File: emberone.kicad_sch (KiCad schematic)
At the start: 22 parts, among them J1 Screw Terminal, J2 Screw Terminal

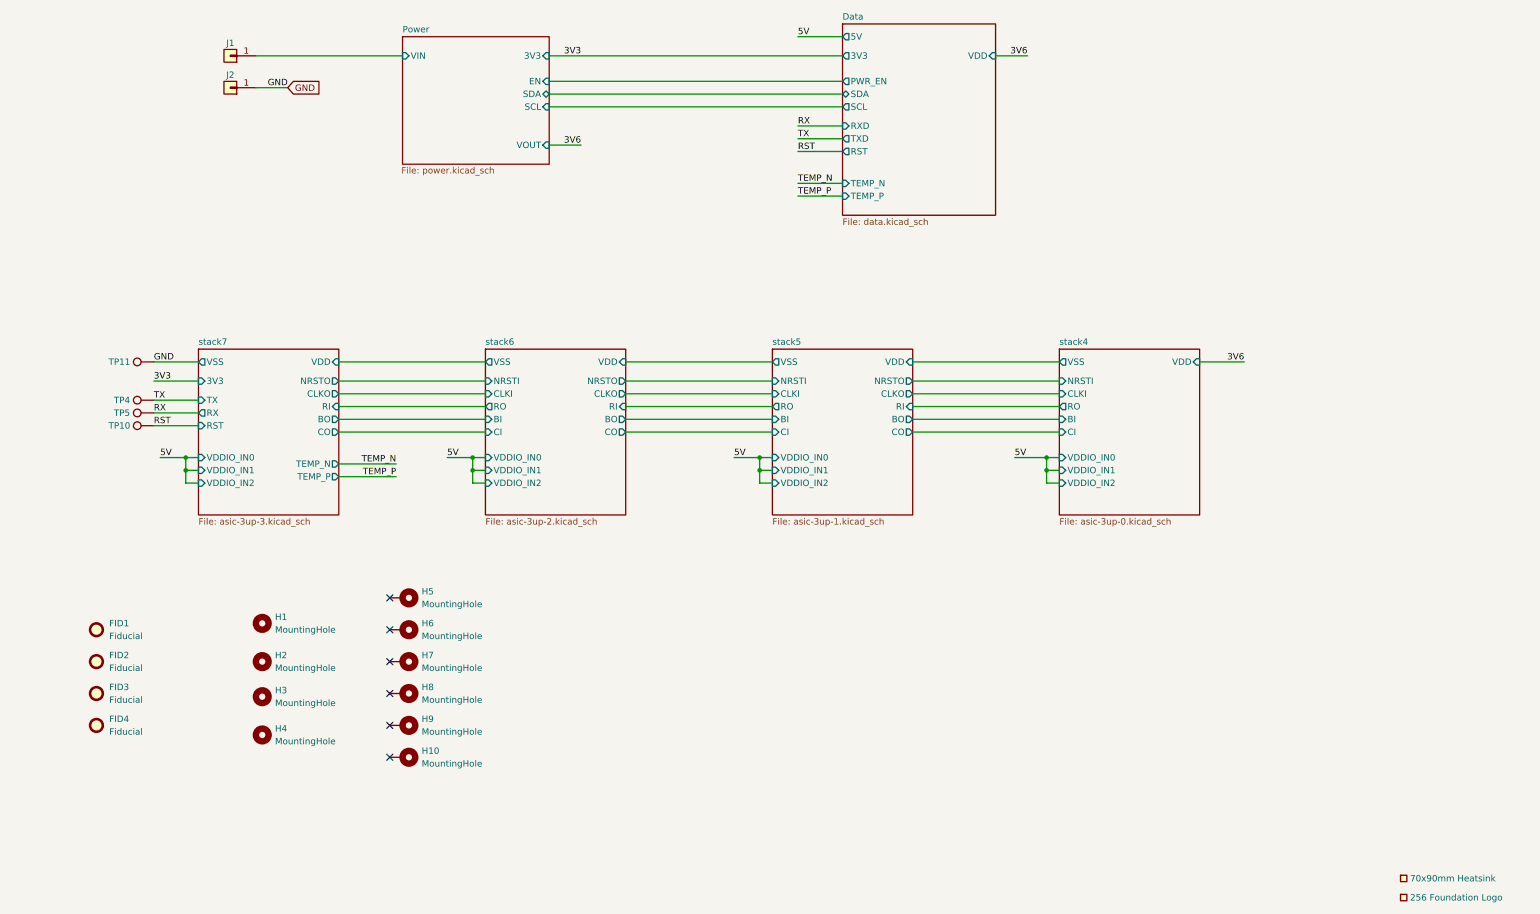
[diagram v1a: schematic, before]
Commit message: switch schematic to TPS546D24S regulator. get pcb mostly synced
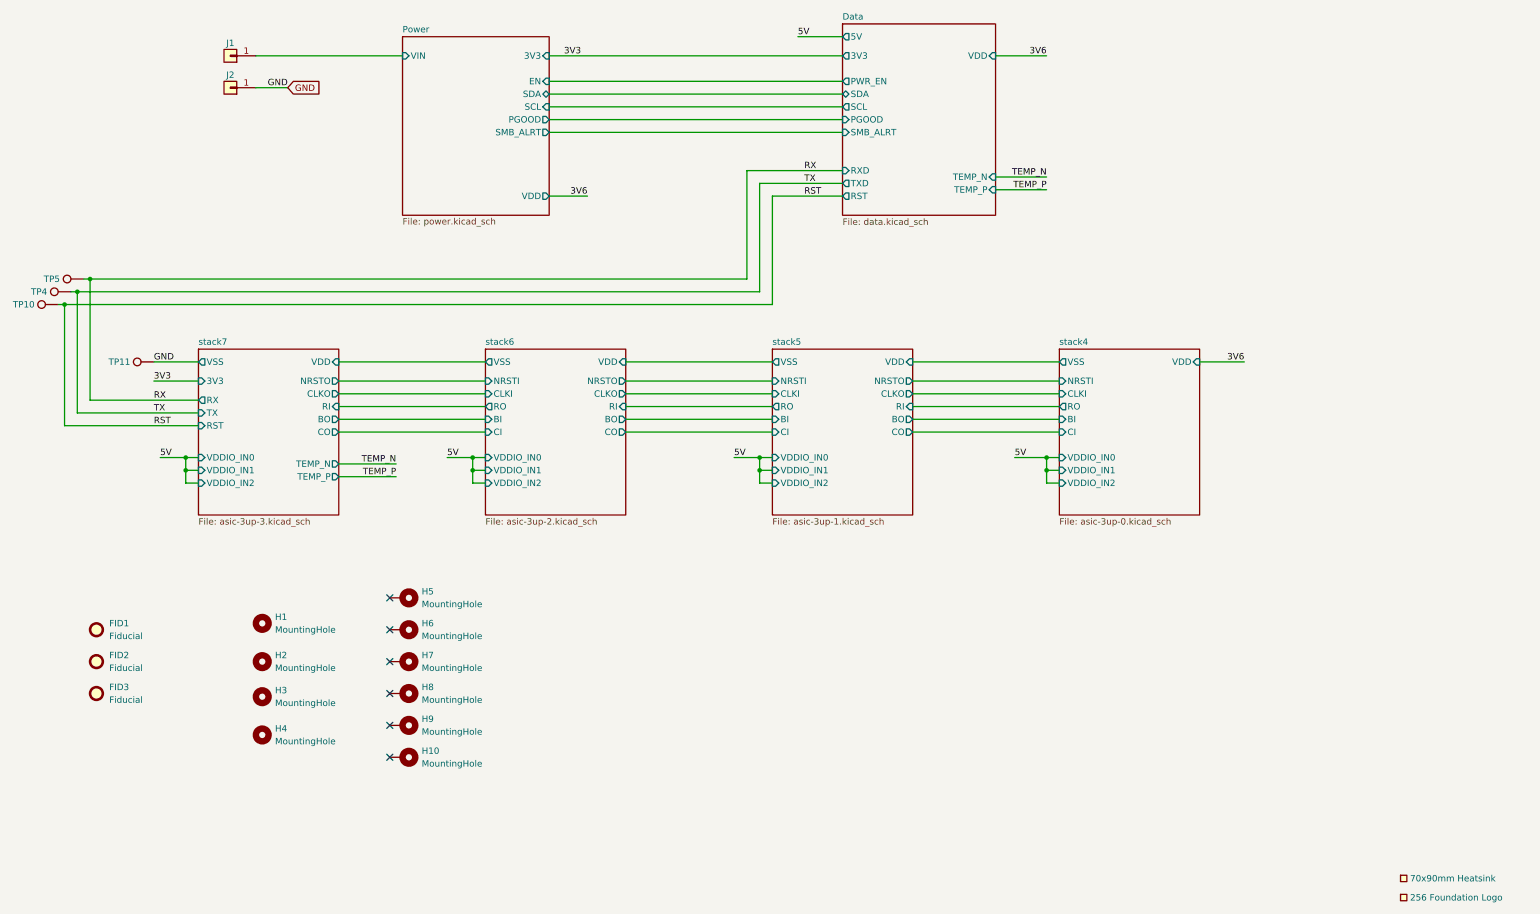
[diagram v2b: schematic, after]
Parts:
- removed FID4: Fiducial, emberone:Fiducial_1mm_Mask2mm, symbol Mechanical:Fiducial
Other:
- sheet Data ports: added PGOOD, SMB_ALRT; removed none
- sheet Power ports: added PGOOD, SMB_ALRT, VDD; removed VOUT
- moved on the sheet: TP10, TP4, TP5

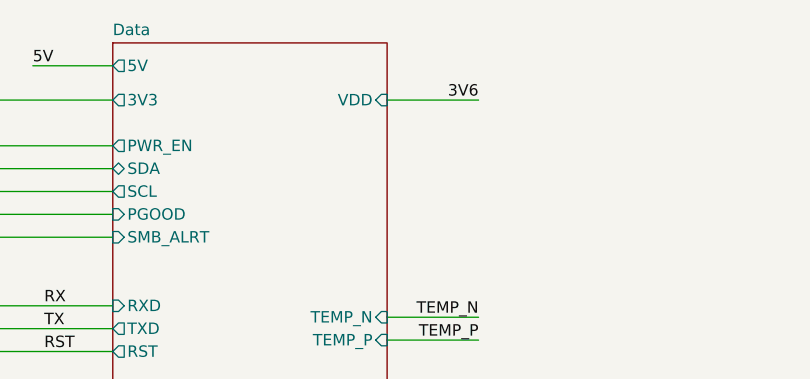
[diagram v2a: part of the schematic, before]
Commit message: mostly done routing
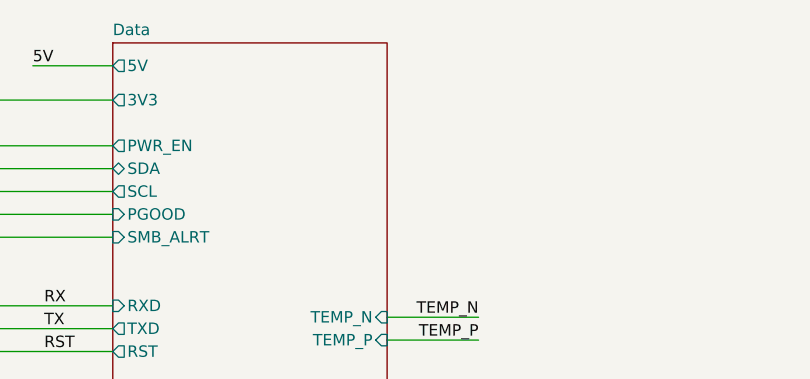
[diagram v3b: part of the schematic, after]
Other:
- sheet Data ports: added none; removed VDD
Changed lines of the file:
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@@
-	(wire
-		(pts
-			(xy 269.24 82.55) (xy 279.4 82.55)
-		)
-		(stroke
-			(width 0)
-			(type default)
-		)
-	)
 	(wire
 		(pts
@@
 			)
 			(justify left bottom)
-		)
-	)
-	(label "3V6"
-		(at 279.4 82.55 180)
-		(effects
-			(font
-				(size 1.27 1.27)
-			)
-			(justify right bottom)
 		)
 	)
@@
 			)
 		)
-		(pin "VDD" input
-			(at 269.24 82.55 0)
-			(effects
-				(font
-					(size 1.27 1.27)
-				)
-				(justify right)
-			)
-		)

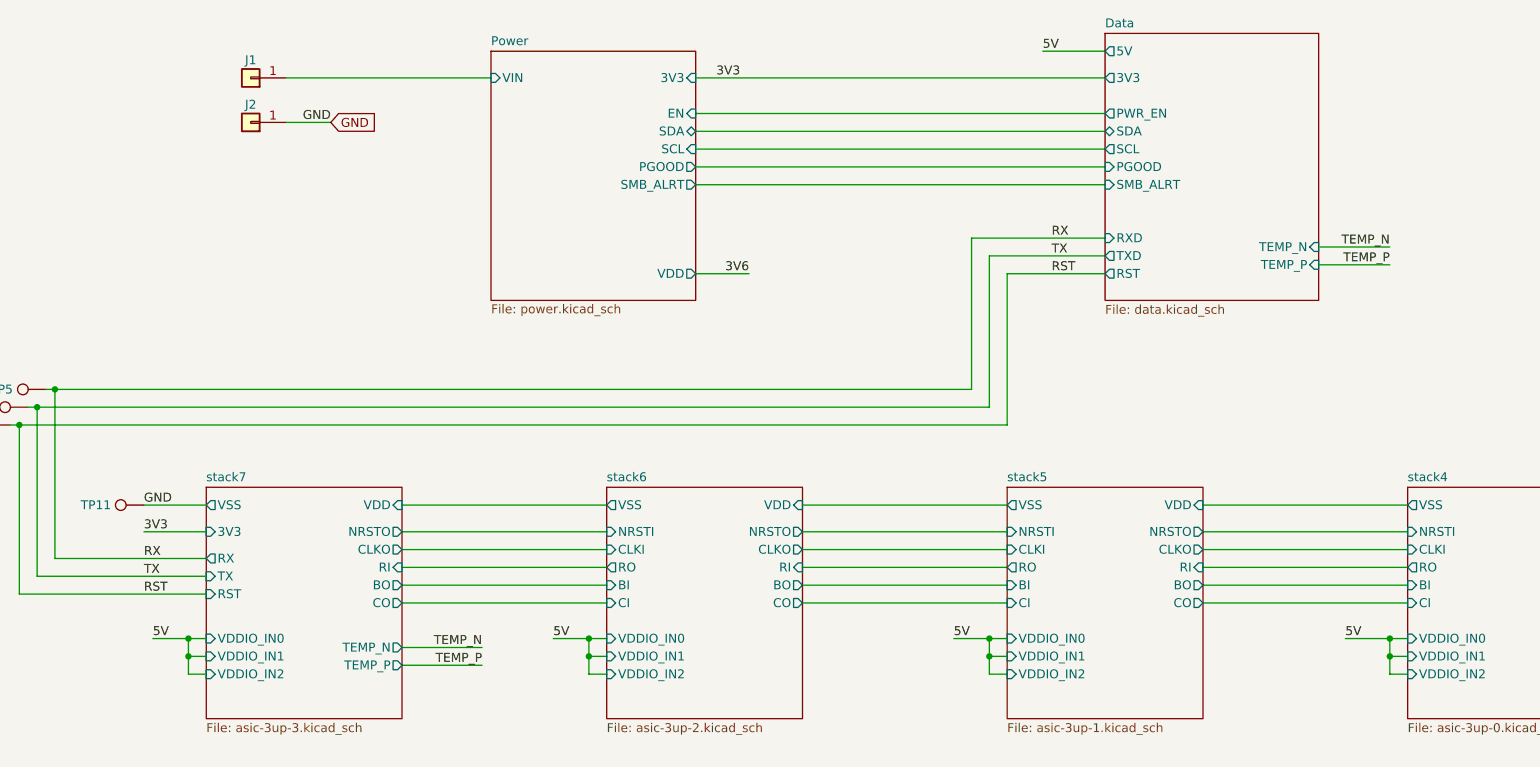
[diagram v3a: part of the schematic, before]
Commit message: Added 5V Load switch TPS22919 for #52
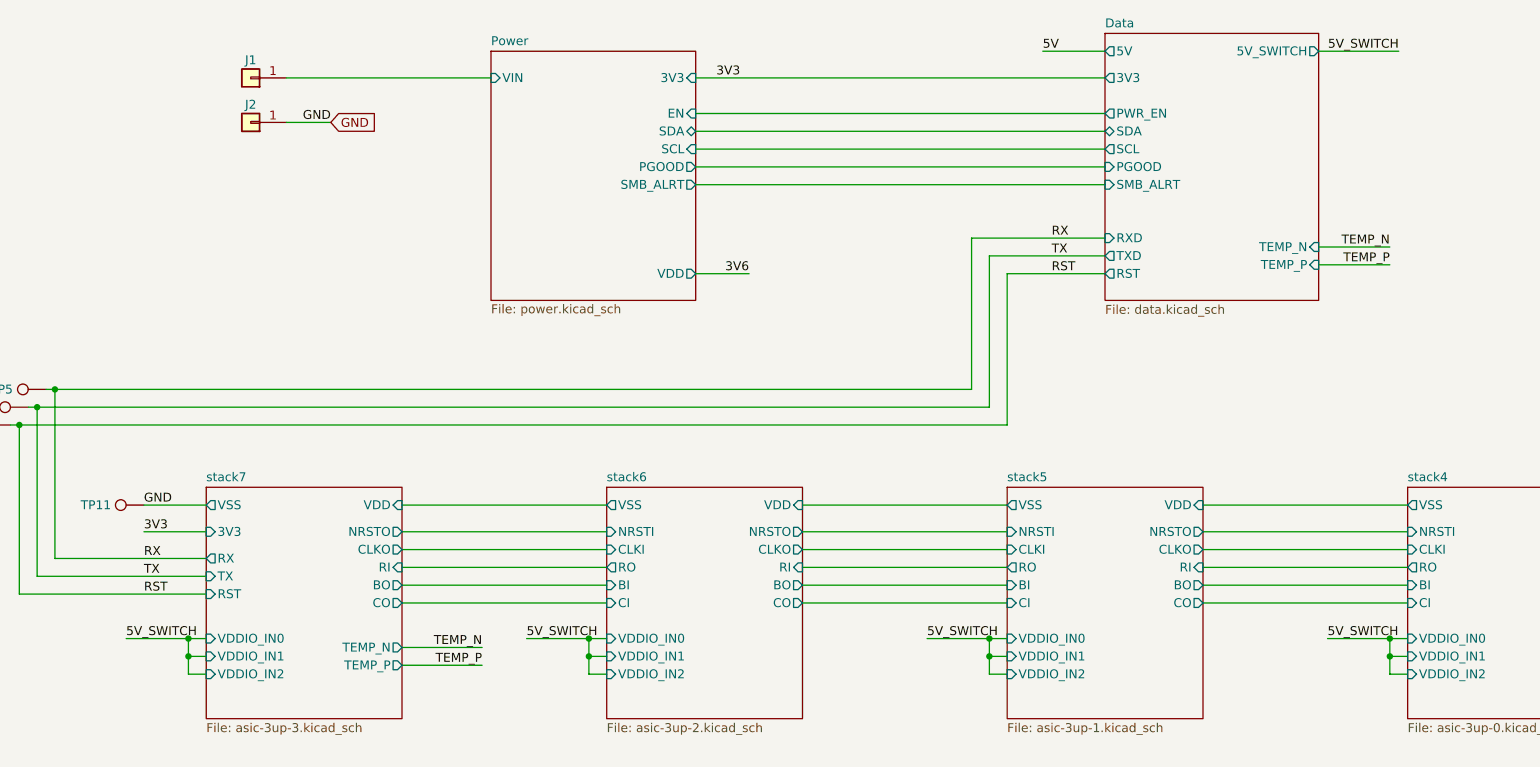
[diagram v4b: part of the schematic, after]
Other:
- sheet Data ports: added 5V_SWITCH; removed none

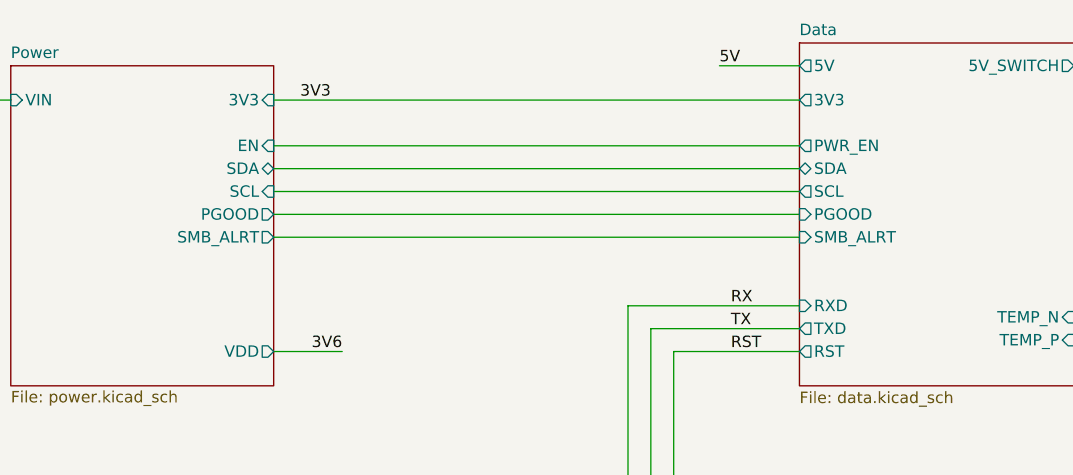
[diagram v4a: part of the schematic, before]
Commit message: cleanup traces, add optional accessory port, update render
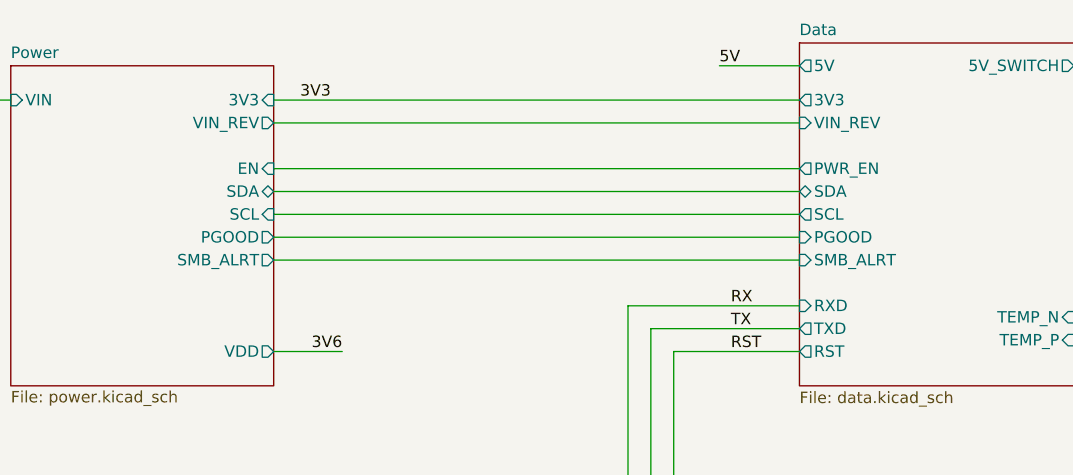
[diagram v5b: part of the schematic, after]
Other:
- sheet Data ports: added VIN_REV; removed none
- sheet Power ports: added VIN_REV; removed none
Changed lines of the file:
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@@
 	(wire
 		(pts
-			(xy 180.34 95.25) (xy 238.76 95.25)
+			(xy 180.34 97.79) (xy 238.76 97.79)
 		)
 		(stroke
@@
 	(wire
 		(pts
-			(xy 180.34 97.79) (xy 238.76 97.79)
+			(xy 180.34 100.33) (xy 238.76 100.33)
 		)
 		(stroke
@@
 	(wire
 		(pts
-			(xy 180.34 90.17) (xy 238.76 90.17)
+			(xy 180.34 92.71) (xy 238.76 92.71)
 		)
 		(stroke
@@
 	(wire
 		(pts
-			(xy 180.34 87.63) (xy 238.76 87.63)
+			(xy 180.34 90.17) (xy 238.76 90.17)
 		)
 		(stroke
@@
 	(wire
 		(pts
-			(xy 180.34 92.71) (xy 238.76 92.71)
+			(xy 180.34 95.25) (xy 238.76 95.25)
 		)
 		(stroke
@@
 	(wire
 		(pts
+			(xy 180.34 85.09) (xy 238.76 85.09)
+		)
+		(stroke
+			(width 0)
+			(type default)
+		)
+	)
+	(wire
+		(pts
 			(xy 107.95 165.1) (xy 110.49 165.1)
 		)
@@
 		)
 		(pin "SDA" bidirectional
-			(at 180.34 90.17 0)
+			(at 180.34 92.71 0)
 			(effects
 				(font
@@
 		)
 		(pin "SCL" input
-			(at 180.34 92.71 0)
+			(at 180.34 95.25 0)
 			(effects
 				(font
@@
 		)
 		(pin "EN" input
-			(at 180.34 87.63 0)
+			(at 180.34 90.17 0)
 			(effects
 				(font
@@
 		)
 		(pin "PGOOD" output
-			(at 180.34 95.25 0)
+			(at 180.34 97.79 0)
 			(effects
 				(font
@@
 		)
 		(pin "SMB_ALRT" output
-			(at 180.34 97.79 0)
+			(at 180.34 100.33 0)
+			(effects
+				(font
+					(size 1.27 1.27)
+				)
+				(justify right)
+			)
+		)
+		(pin "VIN_REV" output
+			(at 180.34 85.09 0)
 			(effects
 				(font
@@
 		)
 		(pin "SDA" bidirectional
-			(at 238.76 90.17 180)
+			(at 238.76 92.71 180)
 			(effects
 				(font
@@
 		)
 		(pin "SCL" output
-			(at 238.76 92.71 180)
+			(at 238.76 95.25 180)
 			(effects
 				(font
@@
 		)
 		(pin "PWR_EN" output
-			(at 238.76 87.63 180)
+			(at 238.76 90.17 180)
 			(effects
 				(font
@@
 		)
 		(pin "PGOOD" input
-			(at 238.76 95.25 180)
+			(at 238.76 97.79 180)
 			(effects
 				(font
@@
 		)
 		(pin "SMB_ALRT" input
-			(at 238.76 97.79 180)
+			(at 238.76 100.33 180)
 			(effects
 				(font
@@
 			)
 		)
+		(pin "VIN_REV" input
+			(at 238.76 85.09 180)
+			(effects
+				(font
+					(size 1.27 1.27)
+				)
+				(justify left)
+			)
+		)

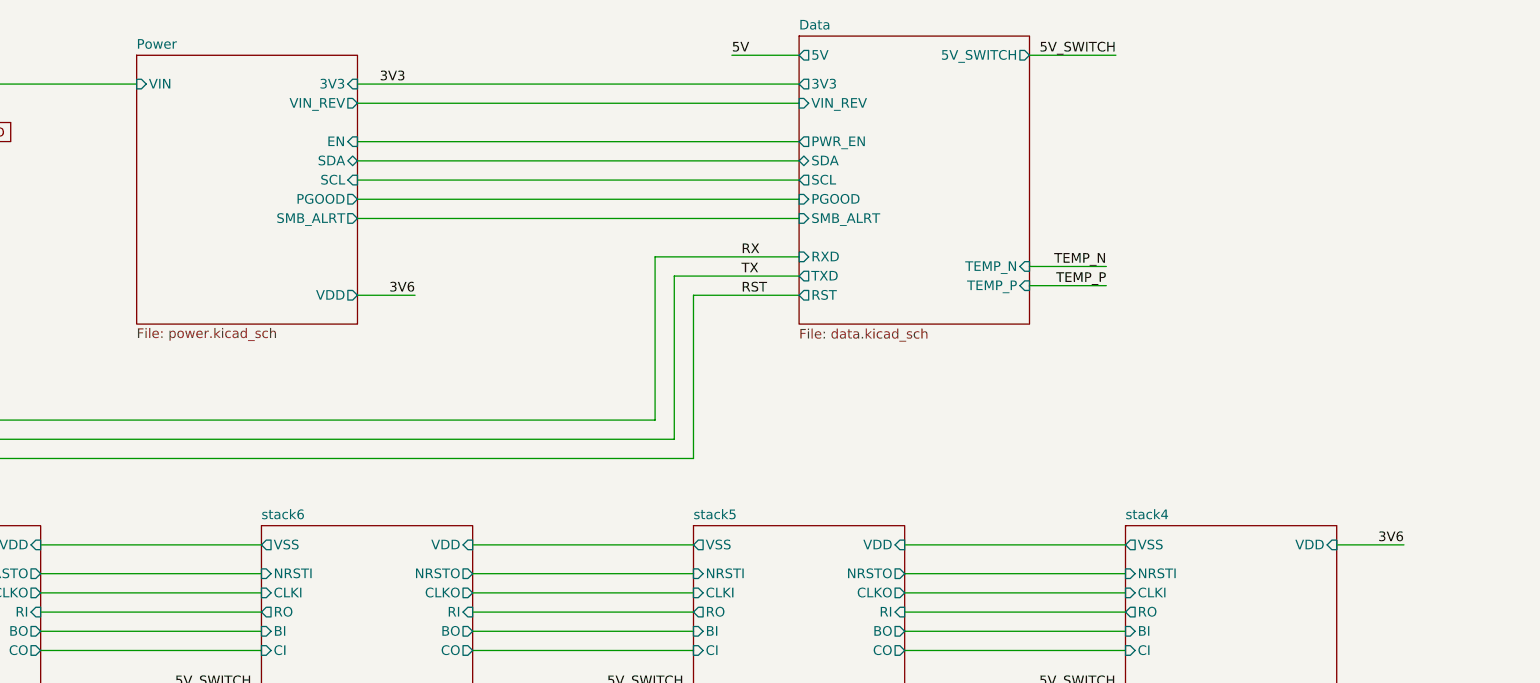
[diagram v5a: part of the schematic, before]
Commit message: add 3V3 to accessory port. add checked gerbers. regenerate render
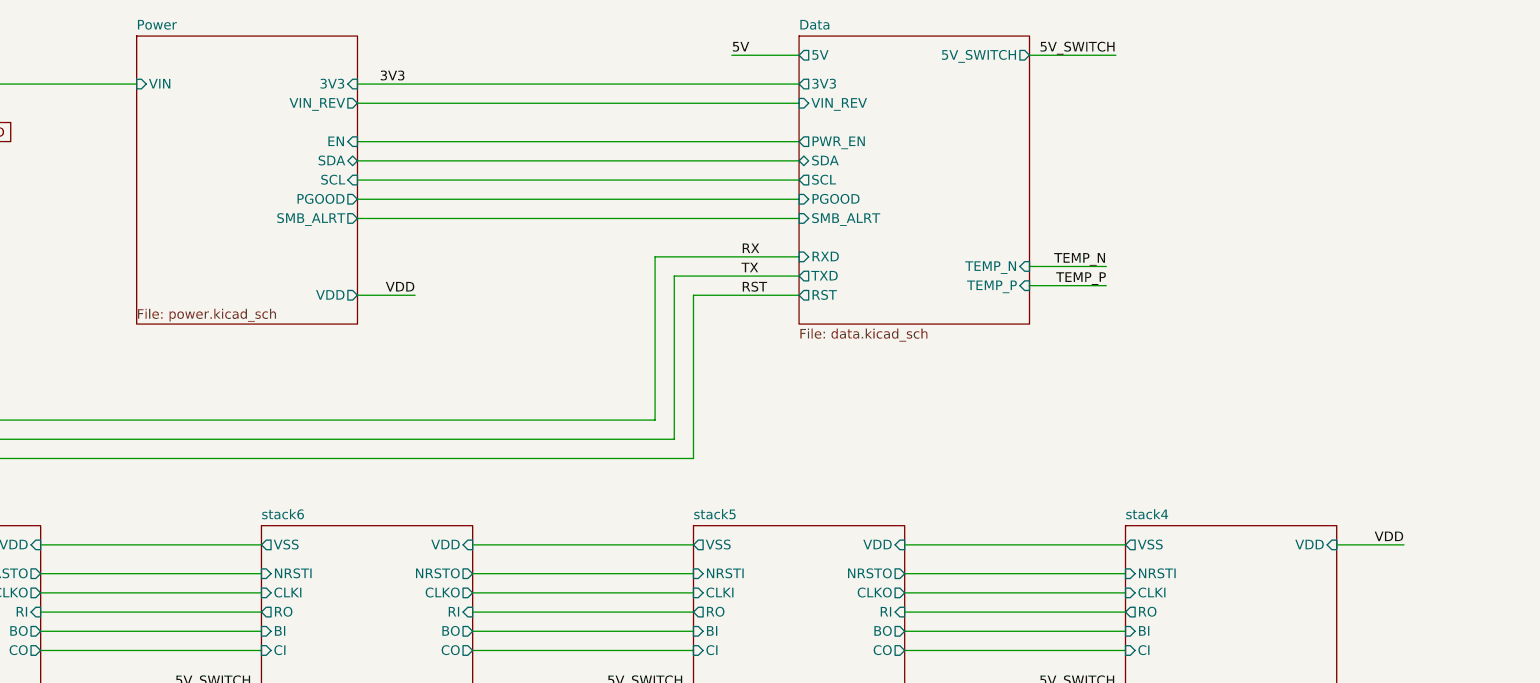
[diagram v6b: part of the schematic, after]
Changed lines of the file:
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@@
 		)
 	)
-	(label "3V6"
+	(label "VDD"
 		(at 318.77 143.51 180)
 		(effects
@@
 		)
 	)
-	(label "3V6"
+	(label "VDD"
 		(at 187.96 110.49 180)
 		(effects
@@
 	)
 	(sheet
-		(at 151.13 78.74)
-		(size 29.21 35.56)
+		(at 151.13 76.2)
+		(size 29.21 38.1)
 		(exclude_from_sim no)
 		(in_bom yes)
@@
 		)
 		(property "Sheetname" "Power"
-			(at 151.13 78.0284 0)
+			(at 151.13 75.4884 0)
 			(effects
 				(font
@@
 		)
 		(property "Sheetfile" "power.kicad_sch"
-			(at 151.13 114.808 0)
-			(effects
-				(font
+			(at 151.13 112.268 0)
+			(effects
+				(font

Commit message: bump version to v6
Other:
- company: (none) -> 256Foundation
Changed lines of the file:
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@@
 	(title_block
 		(title "emberOne/00")
-		(date "2025-09-17")
-		(rev "5")
+		(date "2026-02-17")
+		(rev "v6")
+		(company "256Foundation")
+		(comment 1 "OHL-S-2.0")
 	)
 	(junction
